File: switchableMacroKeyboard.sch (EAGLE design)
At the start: 30 parts

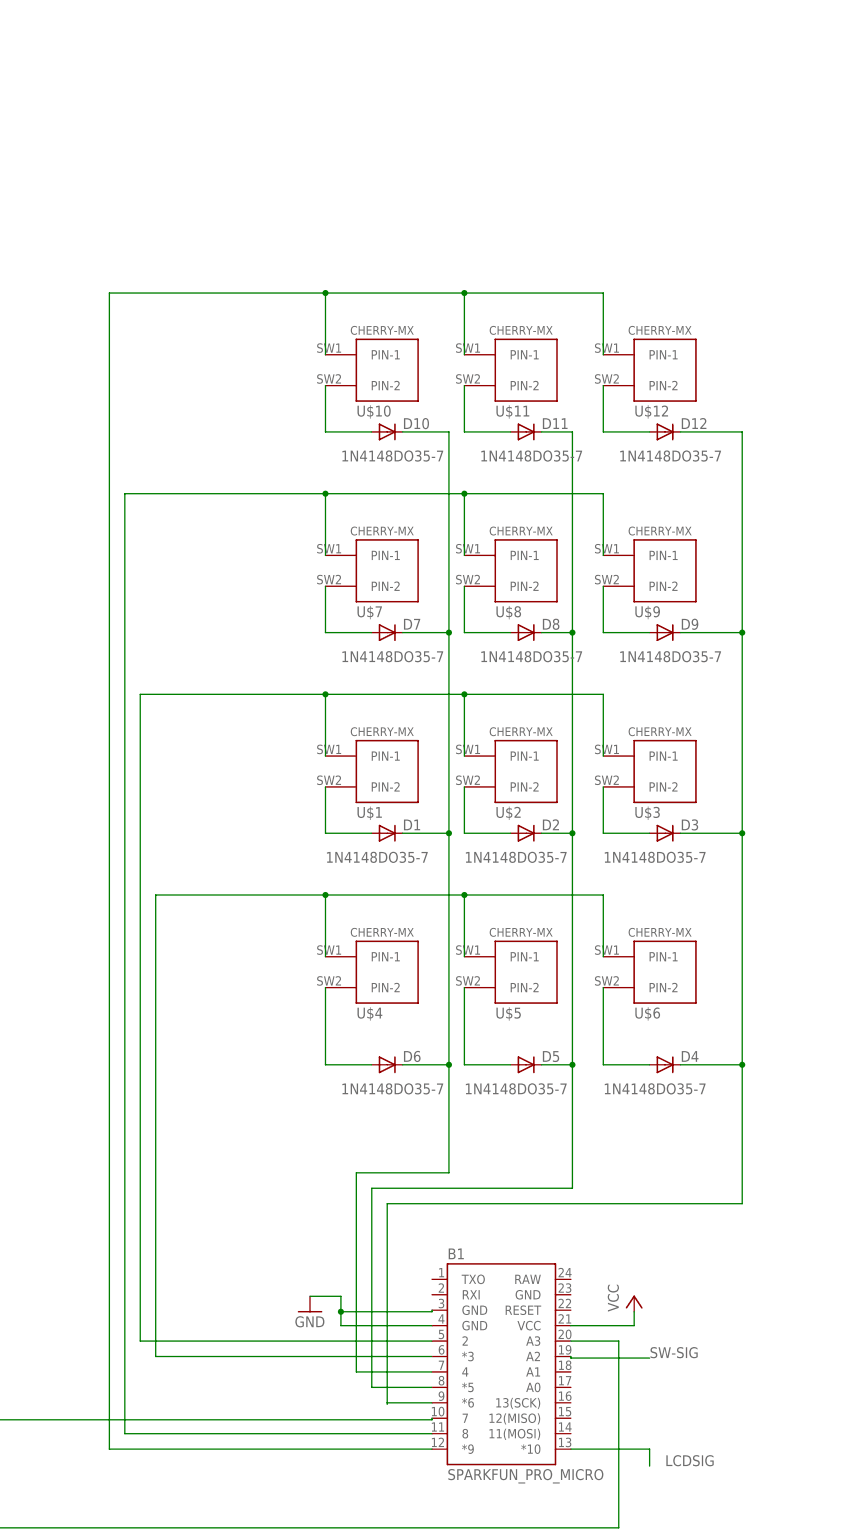
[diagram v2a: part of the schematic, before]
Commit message: Changed to tact switches.
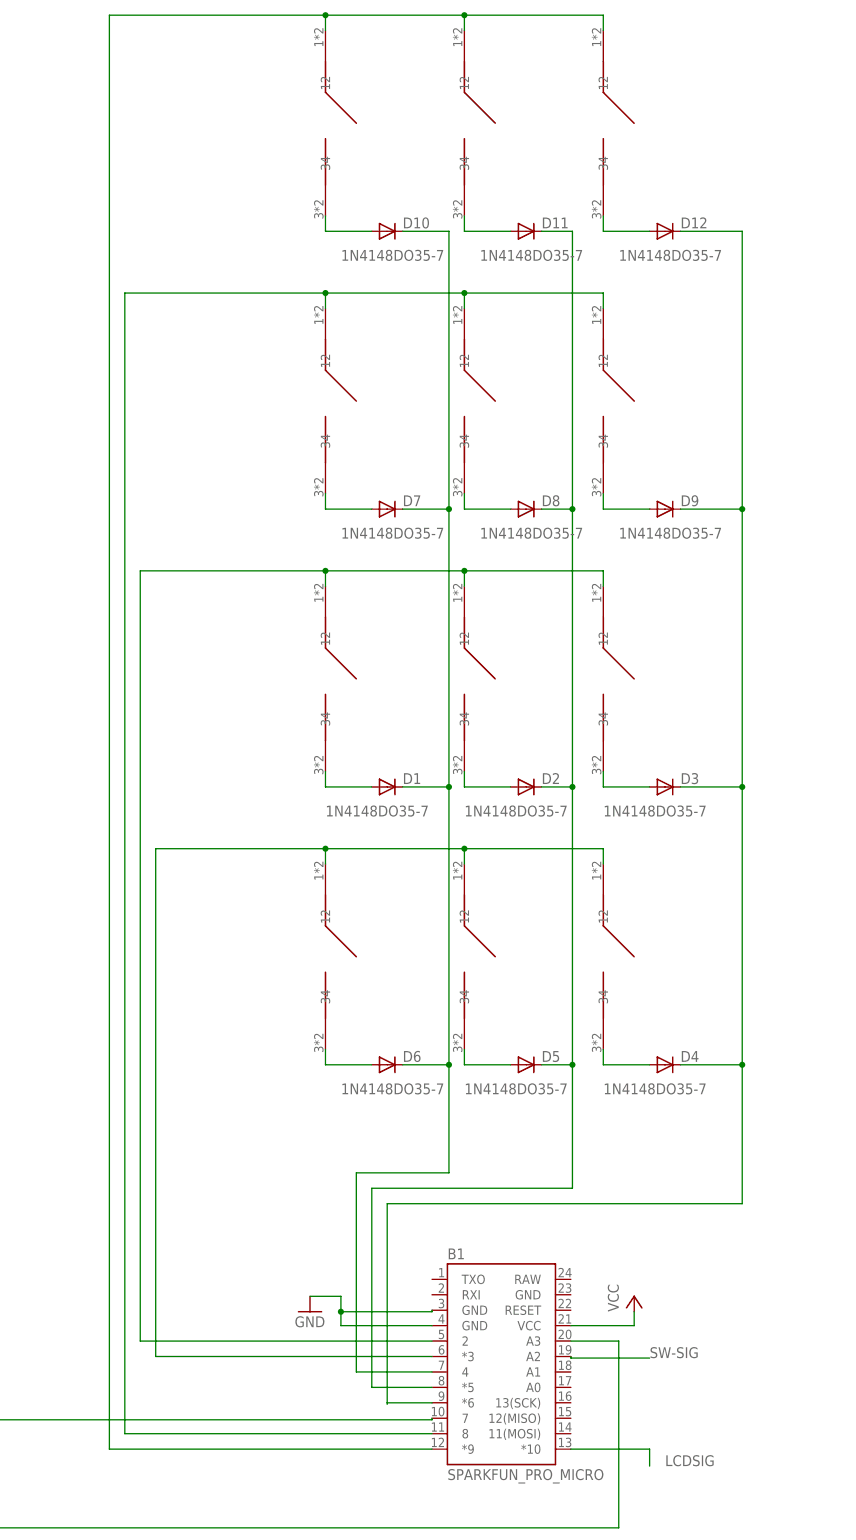
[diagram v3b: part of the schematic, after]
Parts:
- U$1, U$10, U$11, U$12, U$2, U$3, U$4, U$5, U$6, U$7, U$8, U$9: value CHERRY-MX -> TACT-PTS526-SMG15-SMTR2-LFS; device cherrymx:CHERRY-MX -> ARNEInput:TACT-PTS526-SMG15-SMTR2-LFS
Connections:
- net N$1: now also U$7.12, U$8.12, U$9.12; no longer U$1.PIN-1, U$2.PIN-1, U$3.PIN-1
- net N$17: now also U$4.12, U$5.12, U$6.12; no longer U$7.PIN-1, U$8.PIN-1, U$9.PIN-1
- net N$18: now also U$4.34; no longer U$7.PIN-2
- net N$19: now also U$5.34; no longer U$8.PIN-2
- net N$2: now also U$10.12, U$11.12, U$12.12; no longer U$4.PIN-1, U$5.PIN-1, U$6.PIN-1
- net N$20: now also U$6.34; no longer U$9.PIN-2
- net N$24: now also U$1.12, U$2.12, U$3.12; no longer U$10.PIN-1, U$11.PIN-1, U$12.PIN-1
- net N$25: now also U$1.34; no longer U$10.PIN-2
- net N$26: now also U$2.34; no longer U$11.PIN-2
- net N$27: now also U$3.34; no longer U$12.PIN-2
- net N$3: now also U$7.34; no longer U$1.PIN-2
- net N$4: now also U$8.34; no longer U$2.PIN-2
- net N$5: now also U$9.34; no longer U$3.PIN-2
- net N$6: now also U$10.34; no longer U$4.PIN-2
- net N$7: now also U$11.34; no longer U$5.PIN-2
- net N$8: now also U$12.34; no longer U$6.PIN-2
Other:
- moved on the sheet: D1, D10, D11, D12, D2, D3, D7, D8, D9

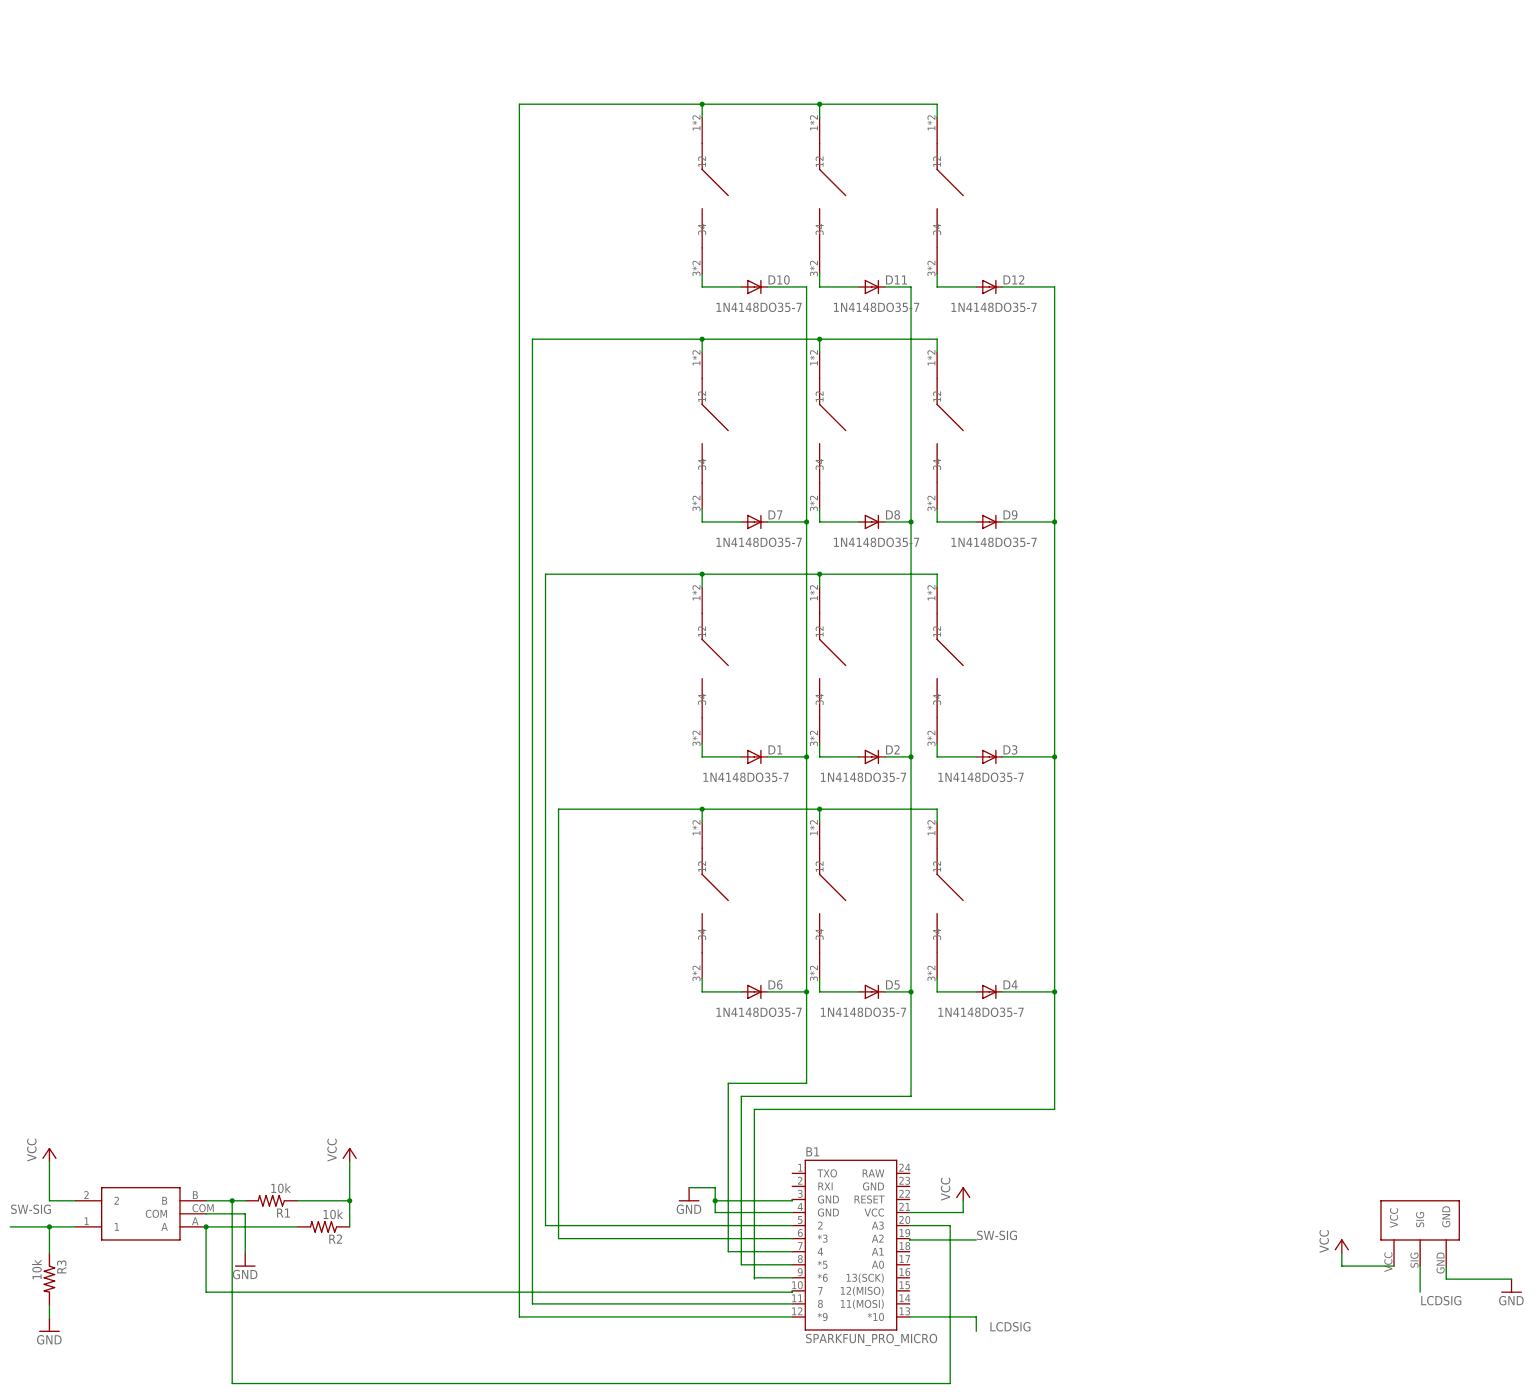
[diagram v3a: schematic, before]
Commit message: Routed the entire board and added pulldown resistors to the columns. To do: sleep on it and order in the morning.
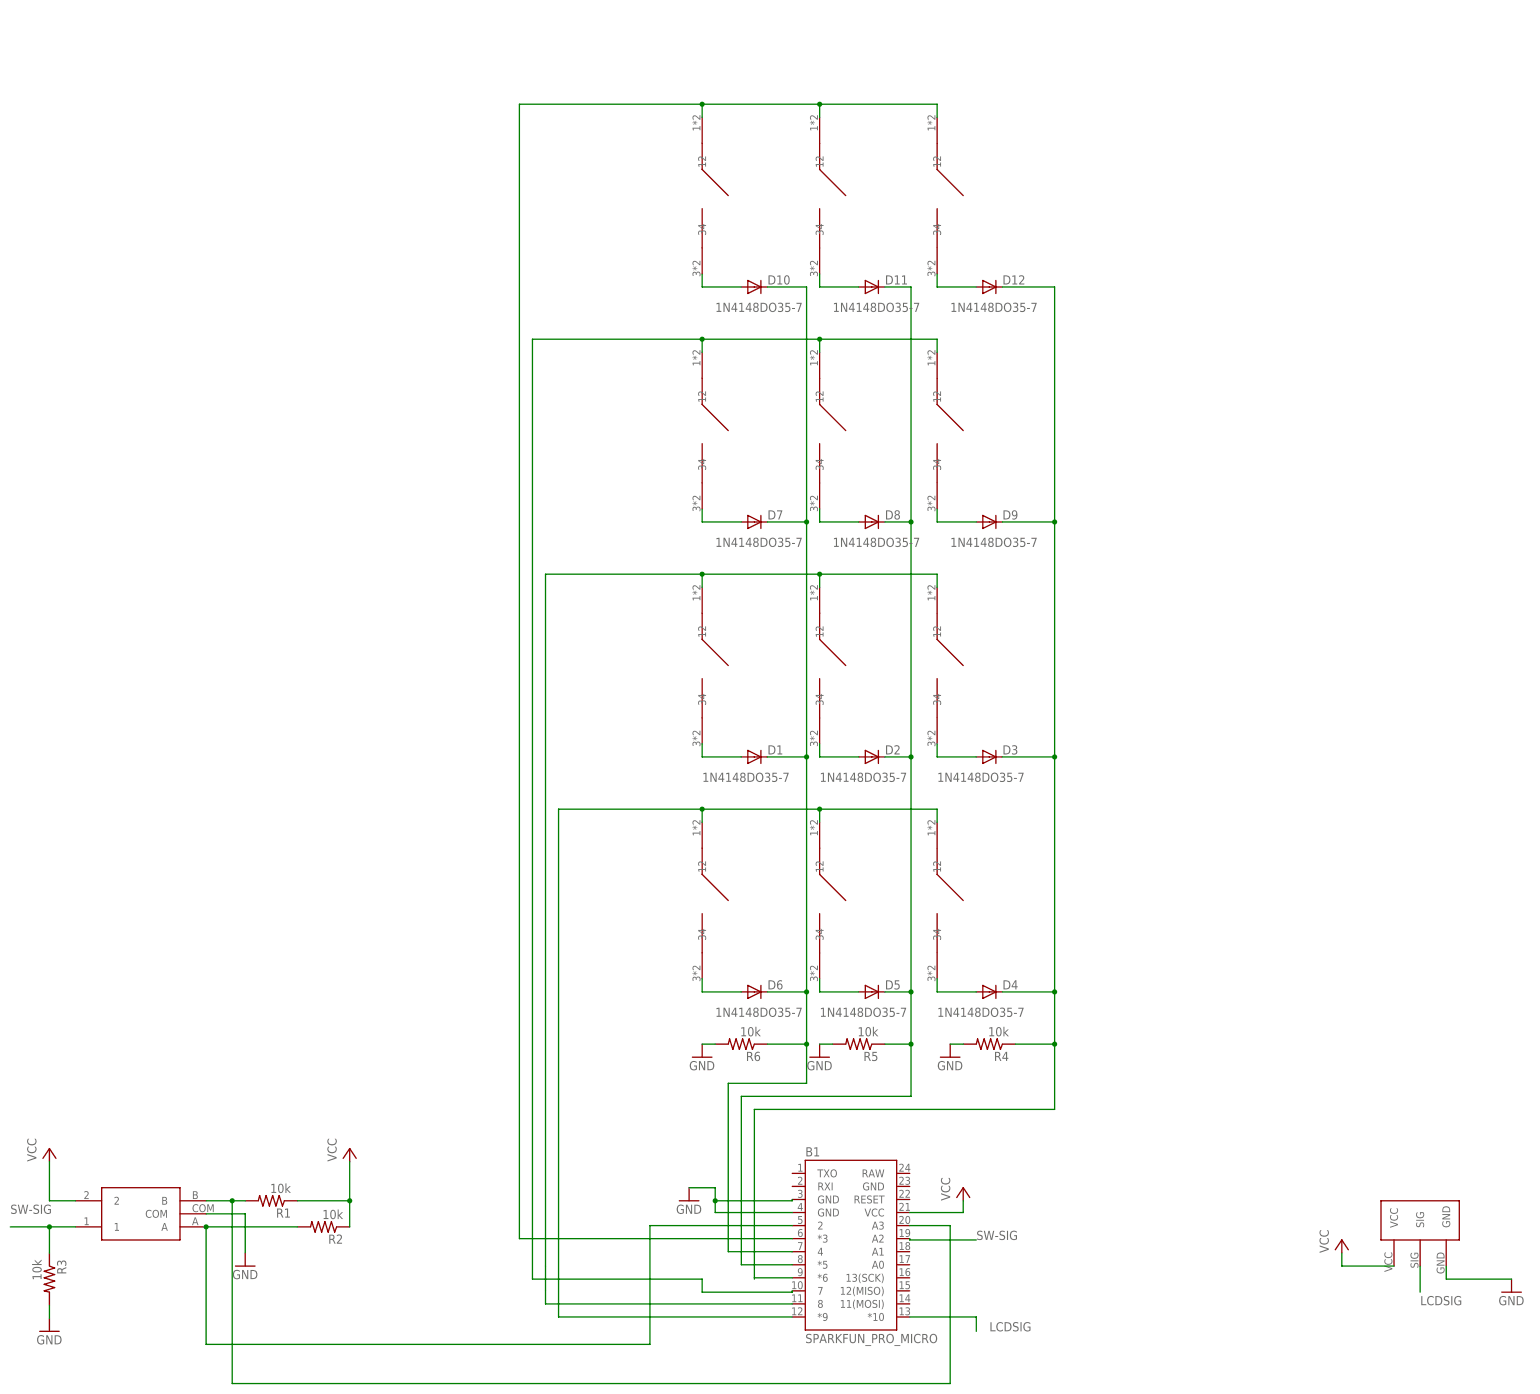
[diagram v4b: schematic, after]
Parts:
- added R4, R5, R6: 10k, rcl:R-US_0207/10
- renumbered U$1 to 00, U$10 to 30, U$11 to 31, U$12 to 32, U$2 to 01, U$3 to 02, U$4 to 10, U$5 to 11, U$6 to 12, U$7 to 20, U$8 to 21, U$9 to 22
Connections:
- removed net N$1: 20.12, 21.12, 22.12, B1.2
- new net N$10: 20.12, 21.12, 22.12, B1.8
- net GND: now also R4.2, R5.2, R6.2
- net N$12: now also B1.2; no longer B1.7
- net N$17: now also B1.7; no longer B1.8
- net N$2: now also B1.*9; no longer B1.*3
- net N$22: now also R5.1
- net N$24: now also B1.*3; no longer B1.*9
- net N$28: now also R6.1
- net N$30: now also R4.1
